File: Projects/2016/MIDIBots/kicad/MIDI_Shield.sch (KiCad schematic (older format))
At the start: 32 parts, among them IC1 PC900V, K1 CONN_SERVO_1, P1 MIDI_IN, P2 MIDI_THRU, P3 CONN_MOLEX_POWER, P4 CONN_MIDI_IN, P5 CONN_MIDI_IN, P6 CONN_2, Q1 F12N10L, SW1 SW_PUSHBUTTON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

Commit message: Associated some more footprints, set bypass cap sizes, some renaming
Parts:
- C1: value C -> 100nF; footprint (none) -> discret:C2
- C2, C3: renamed from C?; footprint (none) -> discret:C2
- D1, D4: footprint (none) -> discret:D4
- D5: renamed from D?; Colour (none) -> green
- IC1: footprint DIP6 -> dip_sockets:DIP-6__300_ELL
- K1: footprint (none) -> connect:SIL-3
- P4, P5: footprint (none) -> connect:SIL-2
- P6: value CONN_2 -> CONN_PWM
- R1, R2, R3, R4, R5, R6, R7, R8: footprint (none) -> discret:R4
- R9: renamed from R?; footprint (none) -> discret:R4
- SW1: value SW_PUSHBUTTON -> RESET_BTN
- SW3: value SW_PUSHBUTTON -> SELF_TEST_BTN
- U1: footprint (none) -> dip_sockets:DIP-14__300_ELL

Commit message: - Flipped orientation of MOSFET_PWM output connector  - Added +5V power indicator LED  - Added limiting resistor to DIP switch array  - Relabelled built-in LED
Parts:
- added D6: 5V, led:LED-3MM, symbol LED-RESCUE-MIDI_Shield
- added R10: 330R, discret:R4-LARGE_PADS, symbol R-RESCUE-MIDI_Shield
- added R11: 1k, discret:R4-LARGE_PADS, symbol R-RESCUE-MIDI_Shield
- C1, C2, C3: symbol C -> C-RESCUE-MIDI_Shield
- D1: footprint discret:D4 -> discret:D3
- D2: value LED -> LED_D13; symbol LED -> LED-RESCUE-MIDI_Shield
- D3: symbol LED -> LED-RESCUE-MIDI_Shield
- D5: value LED_PWR_12V -> 12V; symbol LED -> LED-RESCUE-MIDI_Shield
- K1: value CONN_SERVO_1 -> SERVO_1
- P1, P2: symbol DIN_5 -> DIN_5-RESCUE-MIDI_Shield
- P4: value CONN_MIDI_IN -> MIDI_IN
- P5: value CONN_MIDI_IN -> MIDI_THRU
- P6: value CONN_PWM -> D6_PWM; footprint (none) -> connect:SIL-2
- Q1: footprint discret:TO220 -> discret:TO220_VERT
- R1, R2, R3, R4, R5, R6, R7, R8, R9: footprint discret:R4 -> discret:R4-LARGE_PADS; symbol R -> R-RESCUE-MIDI_Shield
- RV1: footprint (none) -> connect:SIL-3; symbol POT -> POT-RESCUE-MIDI_Shield
- SW1, SW3: footprint (none) -> discret:SW_PUSH_SMALL
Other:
- note added: "+5V Power LED"
- moved on the sheet: R5, SW2

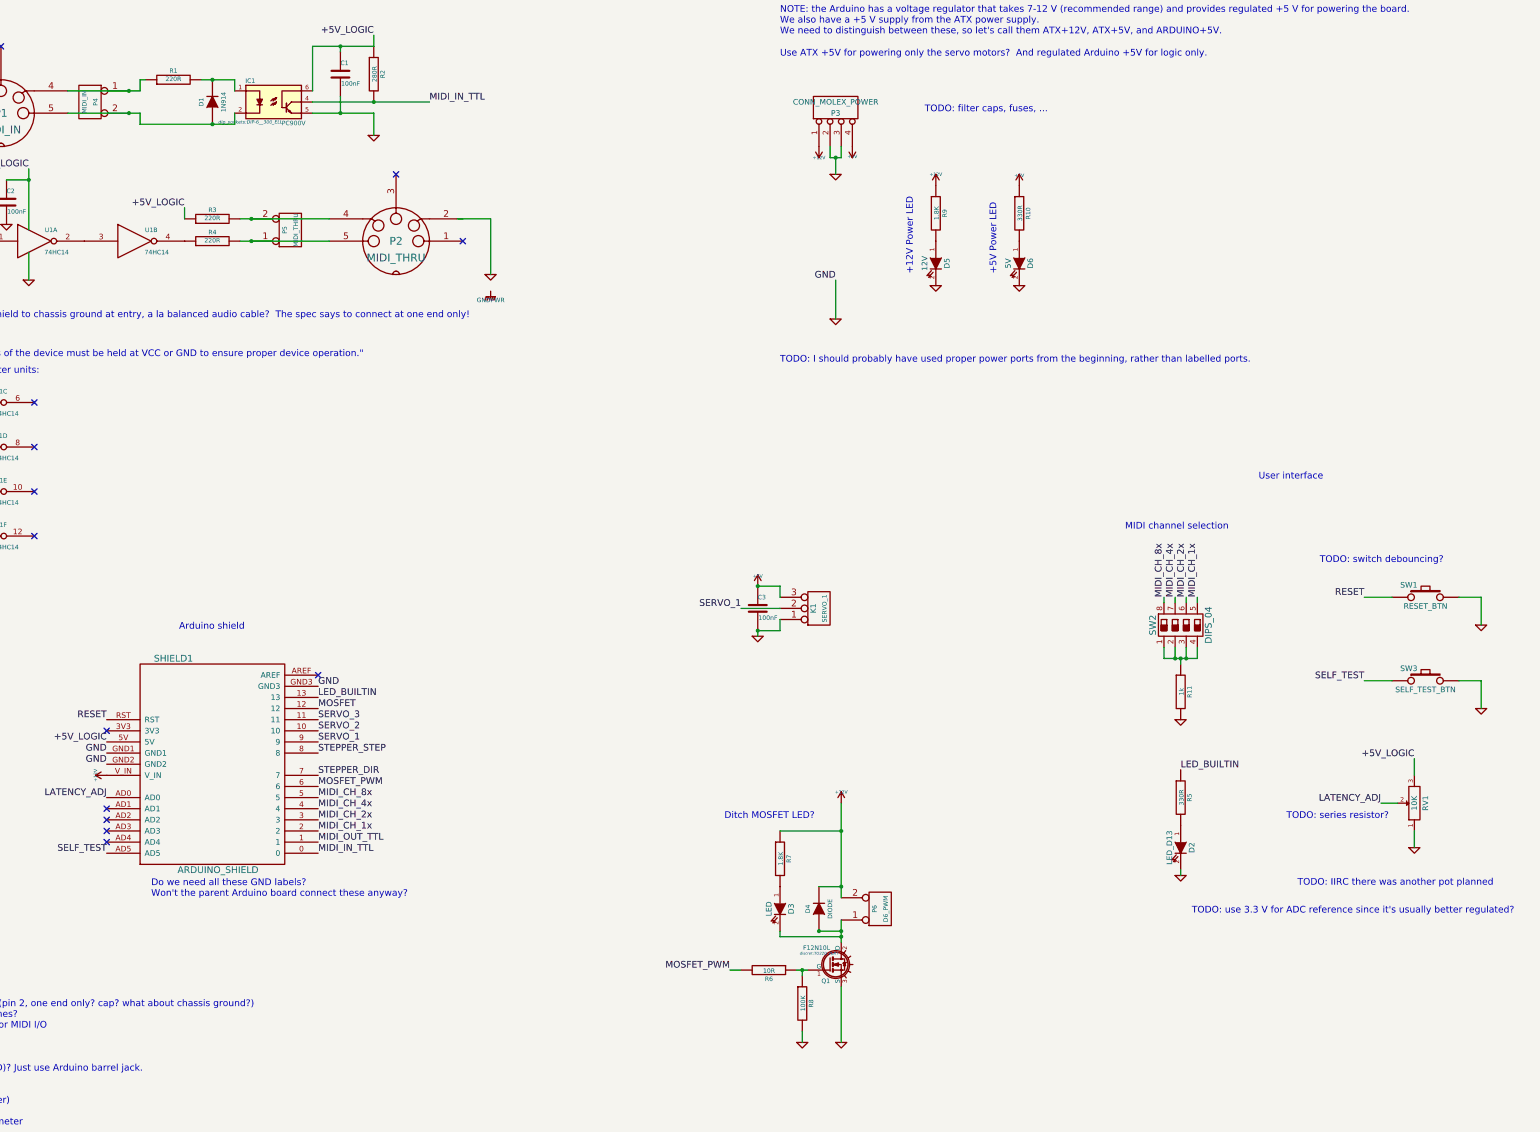
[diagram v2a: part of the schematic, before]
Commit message: - Removed current-limiting resistor on the DIP switches (to save space, and since true protection would only be achieved using a resistor for each pin).  - Added additional servo ports  - Added stepper header  - Added circuitry for second (non-PWM) MOSFET output.  Still want at least a couple more. Maybe should move the stepper output to the other side (using the analog pins) and reassign pins 7 and 8 as MOSFET control pins.
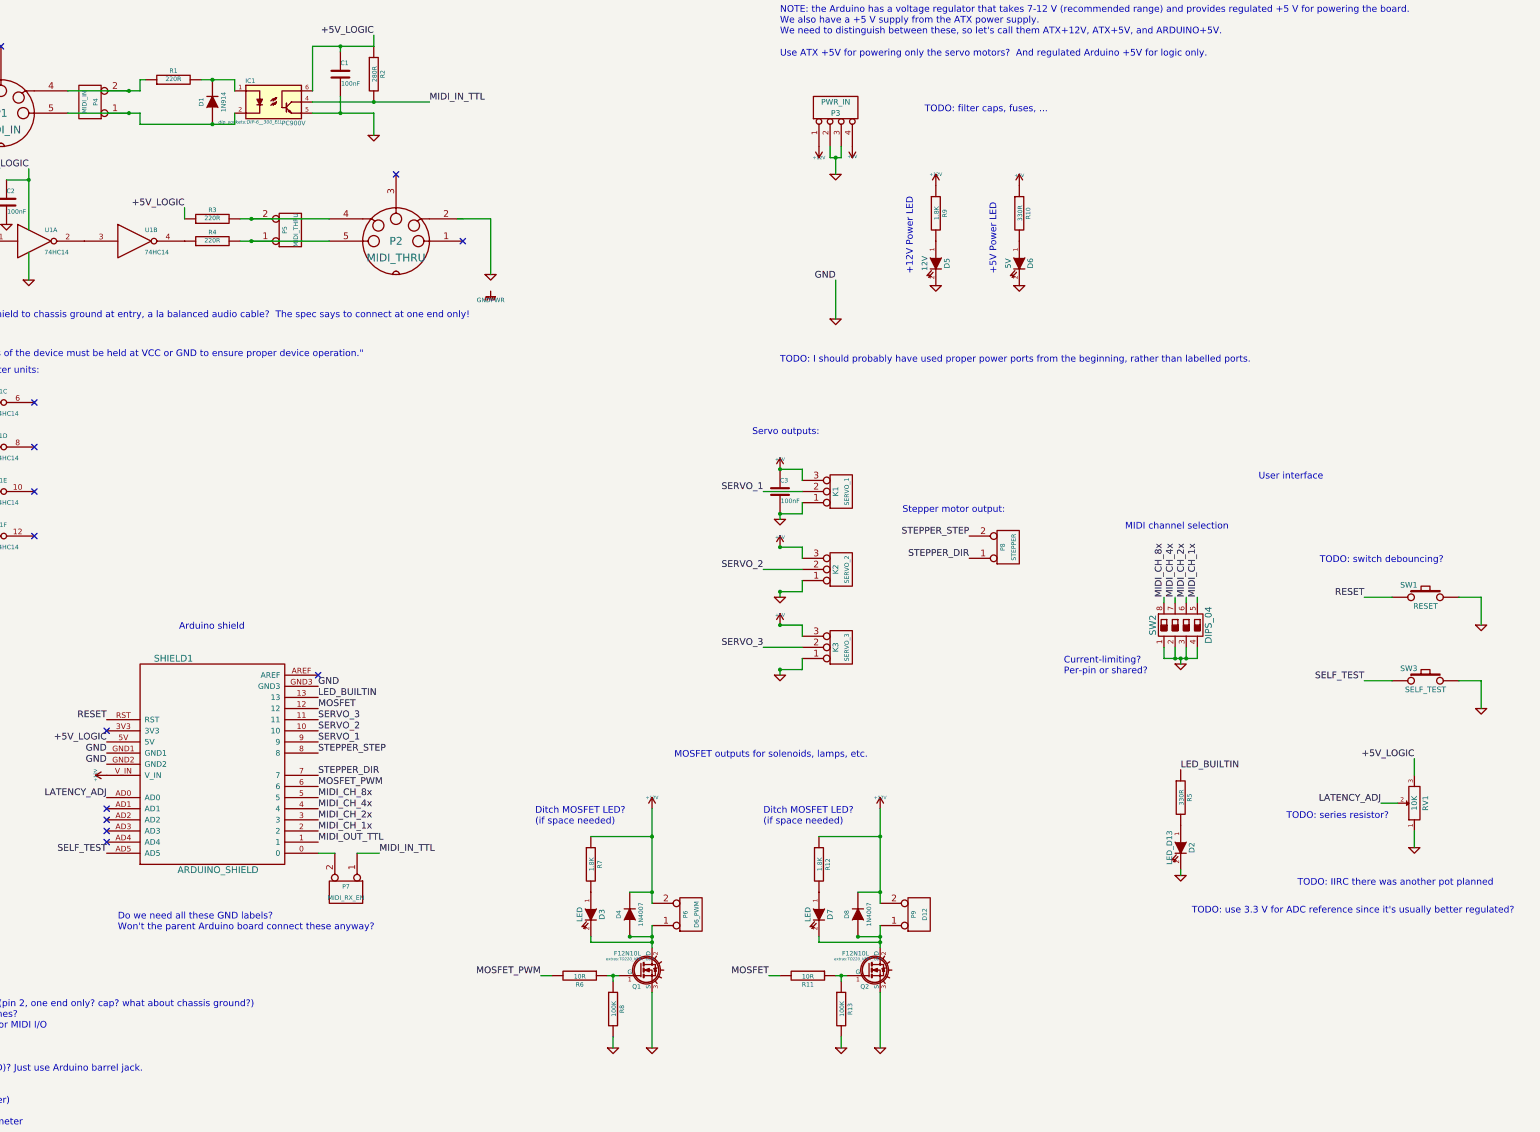
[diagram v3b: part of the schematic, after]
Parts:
- added D7: LED, led:LED-3MM, symbol LED-RESCUE-MIDI_Shield
- added D8: 1N4007, discret:D4, symbol DIODE
- added K2: SERVO_2, connect:SIL-3, symbol CONN_3
- added K3: SERVO_3, connect:SIL-3, symbol CONN_3
- added P7: MIDI_RX_EN, connect:SIL-2, symbol CONN_2
- added P8: STEPPER, connect:SIL-2, symbol CONN_2
- added P9: D12, connect:SIL-2, symbol CONN_2
- added Q2: F12N10L, extras:TO220_VERT_GDS, symbol F12N10L
- added R12: 1.8K, discret:R4-LARGE_PADS, symbol R-RESCUE-MIDI_Shield
- added R13: 100K, discret:R4-LARGE_PADS, symbol R-RESCUE-MIDI_Shield
- D4: value DIODE -> 1N4007
- P3: value CONN_MOLEX_POWER -> PWR_IN
- Q1: footprint discret:TO220_VERT -> extras:TO220_VERT_GDS
- R11: value 1k -> 10R
- SW1: value RESET_BTN -> RESET
- SW3: value SELF_TEST_BTN -> SELF_TEST
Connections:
- net +12V: now also D8.2 (K), P9.2 (PM), R12.1
- net +5V: now also K2.3 (P3), K3.3 (P3)
- net GND: now also SW2.1, SW2.2, SW2.3, SW2.4, K2.1 (P1), K3.1 (P1), Q2.3 (S), R13.2; no longer R11.2
- net MIDI_IN_TTL: now also P7.1 (P1); no longer SHIELD1.0
- net MOSFET: now also R11.2
- net SERVO_2: now also K2.2 (PM)
- net SERVO_3: now also K3.2 (PM)
- net STEPPER_DIR: now also P8.1 (P1)
- net STEPPER_STEP: now also P8.2 (PM)
- net at D1.1 (A), IC1.2, P1.5: now also P4.1 (P1); no longer P4.2 (PM)
- net at P1.4, R1.1: now also P4.2 (PM); no longer P4.1 (P1)
- new net: P7.2 (PM), SHIELD1.0
- new net: Q2.1 (G), R11.1, R13.1
- new net: D7.2 (K), D8.1 (A), P9.1 (P1), Q2.2 (D)
- new net: D7.1 (A), R12.2
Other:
- note added: "Current-limiting?\nPer-pin or shared?"
- note added: "Ditch MOSFET LED?\n(if space needed)"
- note added: "MOSFET outputs for solenoids, lamps, etc."
- note added: "Servo outputs:"
- note added: "Stepper motor output:"
- note removed: "Ditch MOSFET LED?"
- moved on the sheet: C3, D3, D4, K1, P6, Q1, R6, R7, R8

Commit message: Latest schematic and PCB design from work, plus extra libs we might need
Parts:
- added C4, C7: 100nF, discret:C2, symbol C-RESCUE-MIDI_Shield
- added C5, C6: 100uF, capacitors:CP_8x13mm, symbol CP
- added D10, D9: 1N4007, discret:D4, symbol DIODE
- added F1, F2: 2A, discret:R7, symbol F_Small
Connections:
- net +12V: now also C4.1, C5.1, D9.2 (K), F1.1; no longer P3.1 (P1)
- net +5V: now also C6.1, C7.1, D10.2 (K), F2.2; no longer P3.4 (P4)
- net GND: now also C4.2, C5.2, C6.2, C7.2, D10.1 (A), D9.1 (A)
- new net: F1.2, P3.1 (P1)
- new net: F2.1, P3.4 (P4)
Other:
- note added: "Power input, filtering, and protection:"
- note removed: "TODO: filter caps, fuses, ..."
- moved on the sheet: D5, D6, R10, R9

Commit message: - Updated a number of logical component symbols to the new ones, having got a more recent version of KiCAD working on my Debian systems.  - Also updated physical footprint layouts, although this turned out to be a very risky business, as some of the new components have different pin mappings!  Notably, this caused DIODE objects to end up with the wrong polarity on the PCB layout!  LEDs have also flipped around.  Sheesh.  There may still be uncorrected errors arising from this!  - Re-tidied layout (a number of new footprints are rotated 90 degrees from the old ones).
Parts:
- C1, C2, C3, C4, C7: footprint discret:C2 -> Capacitors_ThroughHole:C_Rect_L7_W2.5_P5
- C5, C6: footprint capacitors:CP_8x13mm -> Capacitors_ThroughHole:C_Radial_D7.5_L11.2_P2.5
- D1: footprint discret:D3 -> Discret:D3; symbol DIODE -> D
- D10, D4, D8, D9: footprint discret:D4 -> Discret:D4; symbol DIODE -> D
- D2, D3, D5, D6, D7: footprint led:LED-3MM -> LEDs:LED-3MM; symbol LED-RESCUE-MIDI_Shield -> Led_Small
- F1, F2: footprint discret:R7 -> Fuse_Holders_and_Fuses:Fuseholder5x20_horiz_open_inline_Type-I
- K1: value SERVO_1 -> SRVO1; footprint connect:SIL-3 -> Pin_Headers:Pin_Header_Straight_1x03
- K2: value SERVO_2 -> SRVO2; footprint connect:SIL-3 -> Pin_Headers:Pin_Header_Straight_1x03
- K3: value SERVO_3 -> SRVO3; footprint connect:SIL-3 -> Pin_Headers:Pin_Header_Straight_1x03
- P4, P5, P6, P8, P9: footprint connect:SIL-2 -> Connect:PINHEAD1-2
- P7: footprint connect:SIL-2 -> Pin_Headers:Pin_Header_Straight_1x02
- Q1, Q2: footprint extras:TO220_VERT_GDS -> TO_SOT_Packages_THT:TO-220_Neutral123_Vertical_LargePads
- R1: symbol R-RESCUE-MIDI_Shield -> R
- RV1: footprint connect:SIL-3 -> Connect:PINHEAD1-3
- SHIELD1: footprint (none) -> arduino_shields:ARDUINO_SHIELD
- SW1, SW3: footprint discret:SW_PUSH_SMALL -> Buttons_Switches_ThroughHole:SW_PUSH_SMALL
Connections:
- net +12V: now also D4.1 (K), D8.1 (K), D9.1 (K); no longer D4.2 (K), D8.2 (K), D9.2 (K)
- net +5V: now also D10.1 (K); no longer D10.2 (K)
- net GND: now also D10.2 (A), D2.1 (K), D5.1 (K), D6.1 (K), D9.2 (A), P2.2; no longer D10.1 (A), D2.2 (K), D5.2 (K), D6.2 (K), D9.1 (A)
- net at IC1.1, R1.2: now also D1.1 (K); no longer D1.2 (K)
- net at IC1.2, P1.5, P4.1 (P1): now also D1.2 (A); no longer D1.1 (A)
- net at R5.2: now also D2.2 (A); no longer D2.1 (A)
- net at P6.1 (P1), Q1.2 (D): now also D3.1 (K), D4.2 (A); no longer D3.2 (K), D4.1 (A)
- net at R7.2: now also D3.2 (A); no longer D3.1 (A)
- net at R9.2: now also D5.2 (A); no longer D5.1 (A)
- net at R10.2: now also D6.2 (A); no longer D6.1 (A)
- net at P9.1 (P1), Q2.2 (D): now also D7.1 (K), D8.2 (A); no longer D7.2 (K), D8.1 (A)
- net at R12.2: now also D7.2 (A); no longer D7.1 (A)
- no-connect marks 14 -> 16
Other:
- note added: "Chris has some 2 A fuses that are 5 mm dia, 20 mm length"
- moved on the sheet: D1, P1, P4, R1

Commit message: Added more MOSFET outputs
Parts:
- added D11, D13: LED, LEDs:LED-3MM, symbol Led_Small
- added D12, D14: 1N4007, Discret:D4, symbol D
- added P10, P11: D12, Connect:PINHEAD1-2, symbol CONN_2
- added Q3, Q4: F12N10L, TO_SOT_Packages_THT:TO-220_Neutral123_Vertical_LargePads, symbol F12N10L
- added R14, R17: 1.8K, discret:R4-LARGE_PADS, symbol R
- added R15, R18: 10R, discret:R4-LARGE_PADS, symbol R
- added R16, R19: 100K, discret:R4-LARGE_PADS, symbol R
- R11, R12, R13: symbol R-RESCUE-MIDI_Shield -> R
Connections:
- net +12V: now also D12.1 (K), D14.1 (K), P10.2 (PM), P11.2 (PM), R14.1, R17.1
- net GND: now also Q3.3 (S), Q4.3 (S), R16.2, R19.2
- net MOSFET_3: now reaches SHIELD1.AD3
- net MOSFET_3: now also R15.2
- net MOSFET_4: now reaches SHIELD1.AD4
- net MOSFET_4: now also R18.2
- net MOSFET renamed MOSFET_2
- net MOSFET_PWM renamed MOSFET_1_PWM
- new net: Q3.1 (G), R15.1, R16.1
- new net: D11.1 (K), D12.2 (A), P10.1 (P1), Q3.2 (D)
- new net: D11.2 (A), R14.2
- new net: Q4.1 (G), R18.1, R19.1
- new net: D13.1 (K), D14.2 (A), P11.1 (P1), Q4.2 (D)
- new net: D13.2 (A), R17.2
- no-connect marks 16 -> 14
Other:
- moved on the sheet: D3, D4, D7, D8, P6, P7, P9, Q1, Q2, R11, R12, R13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

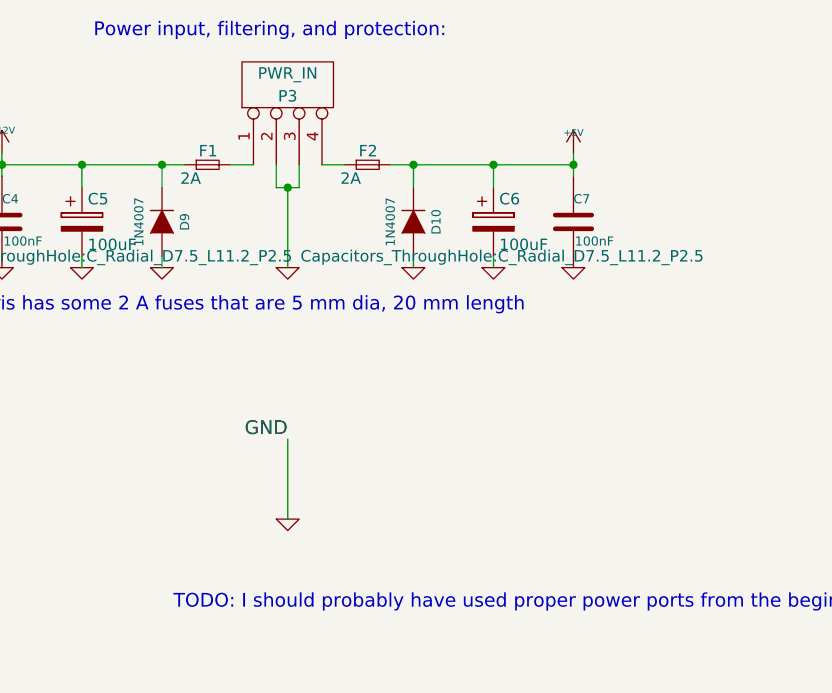
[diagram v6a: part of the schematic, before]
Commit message: Added auxiliary power and ground connectors
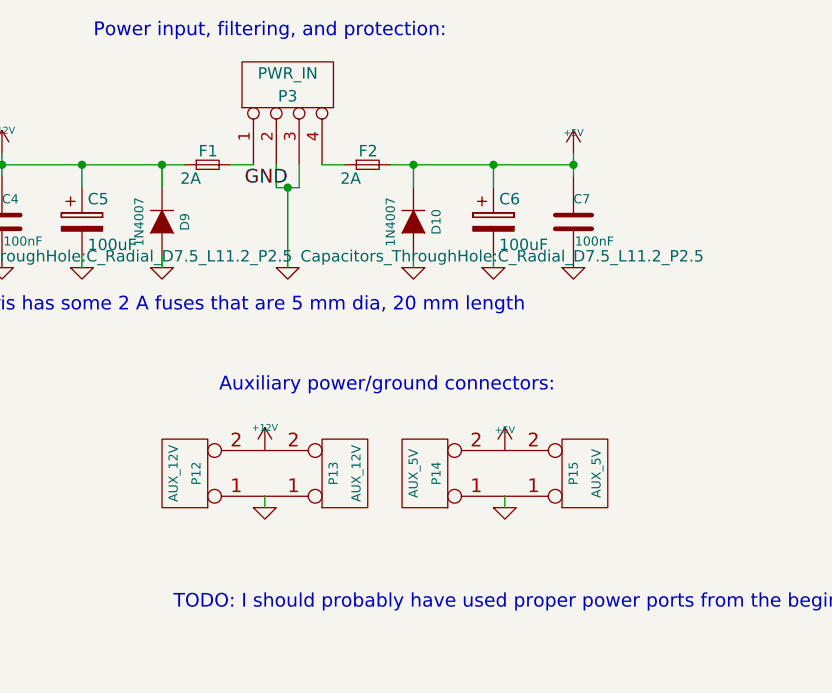
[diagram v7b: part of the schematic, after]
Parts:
- added P12, P13: AUX_12V, Connect:PINHEAD1-2, symbol CONN_2
- added P14, P15: AUX_5V, Connect:PINHEAD1-2, symbol CONN_2
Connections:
- net +12V: now also P12.2 (PM), P13.2 (PM)
- net +5V: now also P14.2 (PM), P15.2 (PM)
- net GND: now also P12.1 (P1), P13.1 (P1), P14.1 (P1), P15.1 (P1)
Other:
- note added: "Auxiliary power/ground connectors:"

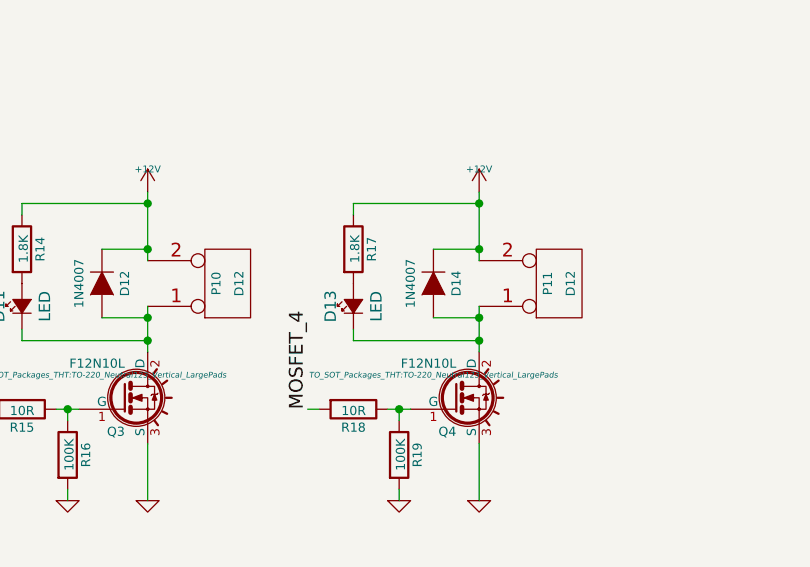
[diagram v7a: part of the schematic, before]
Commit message: Did initial layout for MOSFET outputs 3 and 4, and aux power connectors
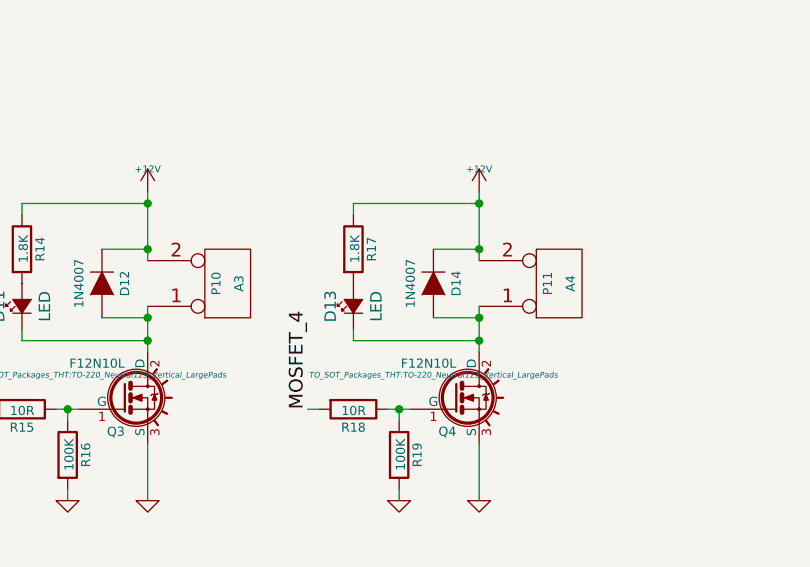
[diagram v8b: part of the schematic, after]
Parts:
- P10: value D12 -> A3
- P11: value D12 -> A4
